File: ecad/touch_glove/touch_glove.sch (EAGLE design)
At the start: 181 parts, among them Q1 MCH3474 4A/30V/50mΩ, Q2 MCH3474 4A/30V/50mΩ, Q3 MCH3474 4A/30V/50mΩ, Q4 MCH3474 4A/30V/50mΩ, Q5 MCH3474 4A/30V/50mΩ, Q6 MCH3474 4A/30V/50mΩ, SW1 4A/28V, Y2 16MHz

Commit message: Rev 2: Complete transformation.  Start by replacing parts with new 3D models and new packages.
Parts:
- removed C135: 0.1uF/50V, PiB_capacitors:0.1UF_SMD-0402_50V-10%
- removed C136: 1uF/25V, PiB_capacitors:1UF_CER_SMD-0402_25V-10%
- added C11, C15, C23: 0.1uF/50V, PiB_capacitors:0.1UF_SMD-0402_50V-10%
- added C19, C24: 10uF/6.3V, PiB_capacitors:10UF_CER_SMD-0402_6.3V-20%
- added C28: 0.1uF/25V, PiB_capacitors:0.1UF_SMD-603_50V-20%
- added R45: 1KΩ, PiB_resistors:1KΩ_SMD-0603_1/10W-5%
- added U1: (no value), PiB:CD74HC4067-SM96_16:1_MUX-DEMUX_16:1-MUX-DEMUX
- added VREG2: 3.3V/250mA, PiB_ic_power:VREG_LINEAR_MCP1700_SOT-23
- added VREG3: 5A/5V, PiB_ic_power:VREG_MIC29501-5.0_LINEAR_ULDO_5A-5VMIC29501-5.0_5A-5V
- added VREG4: (no value), PiB_ic_power:VREG_LINEAR_MCP1700_SOT-23_
- A6: value 2.4GHz/802.11/0.5dBi/3W -> 2.45GHz; device PiB_radio_frequency:ANTENNA_SMD-CHIP_2.4GHZ-0.5DBI-3W -> PiB_radio_frequency:ANTENNA_SMD_CHP-2.45GHZ-0.5DBI-3W
- B2: value Impedence UNBAL/BAL (50Ω/100Ω) -> 50/100
- C10, C120, C123, C126, C14, C18, C22, C27, C37, C39, C43, C44, C97, C99: value 10uF/10V -> 10uF/6.3V; device PiB_capacitors:10UF_CER_SMD-0402_10V-20% -> PiB_capacitors:10UF_CER_SMD-0402_6.3V-20%
- C114: value 22pF/50V -> 22pF/100V; device PiB_capacitors:22PF_SMD-0402_100V-5% -> PiB_capacitors:22PF_CER_SMD-0402-100V-5%
- C115: device PiB_capacitors:0.75PF_SMD-0402_50V-33% -> PiB_capacitors:0.75PF_CER_SMD-0402_50V-33%
- D1, D11, D12, D2, D3, D4, D5: device PiB_discrete_semiconductors:DIODE_GENERAL-PURPOSE_SMD-0402_GP_120MA-75V -> PiB_discrete_semiconductors:DIODE_GENERAL-PURPOSE_SMD-0402_GP_150MA-75V
- DEMUX1: device PiB:CD74HC4067-SM96_16:1_MUX-DEMUX -> PiB:CD74HC4067-SM96_16:1_MUX-DEMUX_SOP-24_16:1-MUX-DEMUX
- JP2: value FTDIPTH-RA -> (none)
- L3, L4: value 10uH/0.38A -> 10uH/380mA
- MCU: value ATMEGA128RFA1 -> ATMEGA128RFA1_VFQFN-64_NO-EXPOSED-PAD; device PiB_ic_microcontrollers:ATMEGA128RFA1_VFQFN-64_EXPOSED-PAD -> PiB_ic_microcontrollers:ATMEGA128RFA1_VFQFN-64_NO-EXPOSED-PAD
- PWM_DRIVER1: device PiB:PCA9685_16-CH_12-BIT_PWM-DRIVER -> PiB:PCA9685_16-CH_12-BIT_PWM-DRIVER_TSSOP-28_PWM-DRIVER_16CH
- R10, R13, R15, R17, R19, R21, R23, R25, R27, R29, R31, R33, R6, R7, R8, R9: value 100Ω -> 100
- R11, R34, R35, R36, R37, R38, R39, R42, R43, R44: value 47KΩ -> 47K
- R40, R41: value 4.7KΩ -> 4.7K
- R48: value 2KΩ -> 2K
- R49: value 1KΩ -> 1K
- VREG1: device PiB_ic_power:VREG_TPS76833_ULDO_FAST-TRANSIENT_1A-3.3VTPS76833QDR_1A-3.3V -> PiB_ic_power:VREG_TPS768XX_ULDO_FAST-TRANSIENT_TPS76833QDR_1A-3.3V
- VREG7: device PiB_ic_power:VREG_LT1764EQ_ULDO_FAST-TRANSIENT_LT1764EQ-1.8_3A-1.8V -> PiB_ic_power:VREG_LT1764EQ_ULDO_FAST-TRANSIENT_LT1764EQ-1.8_3A_1.8V
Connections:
- new net N$33: C15.1, C19.1, L3.2, VREG4.VI
- new net N$34: R45.2, U1.C14
- net AGND: now also C23.2, C24.2; no longer C135.2, C136.2
- net AVCC: now also C23.1, C24.1, VREG4.VO; no longer C135.1, C136.1, L3.2, MCU.AREF
- net BATT_+: now also SW1.S1, U1.S1; no longer SW1.1
- net GND: now also C15.2, C19.2, JP2.GND, VREG4.GND; no longer JP2.6
- net N$10: now also HBRIDGE4.IN1/PH; no longer HBRIDGE4.IN1
- net N$13: now also HBRIDGE3.IN2/EN; no longer HBRIDGE3.IN2
- net N$14: now also HBRIDGE3.IN1/PH; no longer HBRIDGE3.IN1
- net N$19: now also HBRIDGE2.IN2/EN; no longer HBRIDGE2.IN2
- net N$20: now also HBRIDGE2.IN1/PH; no longer HBRIDGE2.IN1
- net N$25: now also HBRIDGE1.IN2/EN; no longer HBRIDGE1.IN2
- net N$26: now also HBRIDGE1.IN1/PH; no longer HBRIDGE1.IN1
- net N$29: now also HBRIDGE5.IN2/EN; no longer HBRIDGE5.IN2
- net N$31: now also HBRIDGE5.IN1/PH; no longer HBRIDGE5.IN1
- net N$44: now also Y2.XTAL2; no longer Y2.2
- net N$45: now also B2.OUT1; no longer B2.OUT2
- net N$46: now also B2.OUT2; no longer B2.OUT1
- net N$48: now also Y2.XTAL1; no longer Y2.1
- net N$50: now also JP2.DTR; no longer JP2.2
- net N$8: now also HBRIDGE4.IN2/EN; no longer HBRIDGE4.IN2
- net RX0: now also JP2.TXO; no longer JP2.4
- net TX0: now also JP2.RXI; no longer JP2.3
- net VBATT: now also SW1.P; no longer SW1.2
- net VCC: now also JP2.VCC; no longer JP2.1
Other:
- moved on the sheet: JP2, L3, VREG7

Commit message: Several more replacements and moved parts such that they are snapped to the grid.
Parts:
- removed C11: 0.1uF/50V, PiB_capacitors:0.1UF_SMD-0402_50V-10%
- removed C28: 0.1uF/25V, PiB_capacitors:0.1UF_SMD-603_50V-20%
- removed R45: 1KΩ, PiB_resistors:1KΩ_SMD-0603_1/10W-5%
- removed U1: (no value), PiB:CD74HC4067-SM96_16:1_MUX-DEMUX_16:1-MUX-DEMUX
- removed VREG2: 3.3V/250mA, PiB_ic_power:VREG_LINEAR_MCP1700_SOT-23
- removed VREG3: 5A/5V, PiB_ic_power:VREG_MIC29501-5.0_LINEAR_ULDO_5A-5VMIC29501-5.0_5A-5V
- C41: value 47uF/10V -> 47uF/6.3V; device PiB_capacitors:47UF_CER_SMD-0805_10V-20% -> PiB_capacitors:47UF_SMD-0805_6.3V-20%
- Q1, Q2, Q3, Q4, Q5, Q6: value MCH3474 4A/30V/50mΩ -> MCH3474 4A/30V; device PiB_discrete_semiconductors:POWER_NCHAN_MCH3474 -> PiB_discrete_semiconductors:POWER_NCHAN_MCH3474_NMOS_4A-30V
- VREG4: value (none) -> 250mA/3.3V
- VREG6: device PiB_ic_power:VREG_LINEAR_FIXED_TL1963A-33_LDO_1.5A-3.3V -> PiB_ic_power:VREG_TL1963A-XX_1.5A_LN_LDO_FAST-TRANSIENT_SOT-223-4_TL1963A-33_1.5A-3.3V
- Y2: value 16MHz -> 16 MHz
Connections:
- removed net N$34: R45.2, U1.C14
- removed net N$44: C113.1, MCU.XTAL1, Y2.XTAL2
- removed net N$48: C112.1, MCU.XTAL2, Y2.XTAL1
- new net N$35: C112.1, MCU.XTAL2, Y2.XTAL2
- new net N$36: C113.1, MCU.XTAL1, Y2.XTAL1
- net BATT_+: no longer U1.S1
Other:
- moved on the sheet: Y2

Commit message: Start and complete much of the 4 layer routing.  All components on board have 3D models.
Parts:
- removed ANALOG_BR: 2PT_GND_TIE, PiB_power_symbols:2PT_GND_TIE
- removed BATT2: BATTERYPTH_HOLES, PiB:BATTERYPTH_HOLES
- removed C1, C3, C4, C5, C6, C7: 0.1uF/50V, PiB_capacitors:0.1UF_SMD-0402_50V-10%
- removed C10, C14, C18, C22, C27: 10uF/6.3V, PiB_capacitors:10UF_CER_SMD-0402_6.3V-20%
- added LIPO1: Molex RA 2mm pitch, PiB_batteries:BATTERY-CONNECTOR_MOLEX_89401_RA-MALE_PITCH-2MM
- AVR_ISP: value AVR ISP -> AVRISP; device PiB_connectors:AVR_SPI_PRG_6NS -> PiB_connectors:AVR_SPI_PRG_6_PTH_VERT-MALE
- FLEX1, FLEX3, FLEX5, FLEX7, FLEX9: device PiB:FLEX-SENSOR10K_2.2IN -> PiB_sensors:FSR_FORCE-SENSATIVE-RESISTOR_PRESS-SENSOR_0530480210_RA-MALE_PITCH-1.25MM
- FLEX100, FLEX2, FLEX4, FLEX6, FLEX8: device PiB:FLEX-SENSOR10K_2.2IN -> PiB_sensors:FSR_FORCE-SENSATIVE-RESISTOR_PRESS-SENSOR_0530470210_VERT-MALE_PITCH-1.25MM
- HBRIDGE1, HBRIDGE2, HBRIDGE3, HBRIDGE4, HBRIDGE5: value DRV8837C -> DRV8837C 1A
- JP2: value (none) -> FTDI; device PiB_connectors:FTDIPTH-RA -> PiB_connectors:FTDI_PTH_RA-MALE
- TEC1, TEC2, TEC3, TEC4, TEC5: value PELTIER -> Molex RA 1.25mm pitch; device PiB:PELTIER-TECNL1025T_1.8A-4.4V_L10.7-W8.8-H2 -> PiB_actuators:PELTIER-TEC_CONNECTOR_0530480210_RA-MALE_PITCH-1.25MM
- VIBE1, VIBE2, VIBE3, VIBE4, VIBE5, VIBE6: value VIBE_MOTOR -> Molex RA 1.25mm pitch; device PiB:VIBE_MOTOR_100MA/3V -> PiB_actuators:VIBE-MOTOR_CONNECTOR_0530480210_RA-MALE_PITCH-1.25MM
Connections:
- removed net BATT_+: BATT2.P, SW1.S1
- removed net C10: DEMUX1.C10
- removed net C11: DEMUX1.C11
- removed net C12: DEMUX1.C12
- removed net C13: DEMUX1.C13
- removed net C8: DEMUX1.C8
- removed net C9: DEMUX1.C9
- removed net N$52: ANALOG_BR.P$1, L4.2
- new net +: LIPO1.+, SW1.S1
- net 1.8V: no longer C10.1, C14.1, C18.1, C22.1, C27.1
- net 3.3V: no longer C1.1, C3.1, C4.1, C5.1, C6.1, C7.1
- net A0: now also DEMUX1.SIG
- net A1: no longer DEMUX1.SIG
- net AGND: now also B2.GND@5, C110.2, C114.2, C115.2, DEMUX1.C10, DEMUX1.C11, DEMUX1.C12, DEMUX1.C13, DEMUX1.C14, DEMUX1.C15, L4.2, MCU.AVSS_RFN, MCU.AVSS_RFP; no longer ANALOG_BR.P$2
- net GND: now also AVR_ISP.GND, LIPO1.-, R1.1, R12.1, R2.1, R3.1, R4.1, R5.1; no longer AVR_ISP.6, B2.GND@5, BATT2.N, C110.2, C114.2, C115.2, MCU.AVSS_RFN, MCU.AVSS_RFP
- net MISO: now also AVR_ISP.MISO; no longer AVR_ISP.1
- net MOSI: now also AVR_ISP.MOSI; no longer AVR_ISP.4
- net N$15: no longer C4.2
- net N$17: no longer C3.2
- net N$2: no longer C6.2
- net N$3: no longer C7.2
- net N$30: no longer C1.2
- net N$4: no longer C5.2
- net NGND: no longer C10.2, C14.2, C18.2, C22.2, C27.2, R1.1, R12.1, R2.1, R3.1, R4.1, R5.1
- net PD4: now also DEMUX1.S0; no longer DEMUX1.S3
- net PD5: now also DEMUX1.S1; no longer DEMUX1.S2
- net PD6: now also DEMUX1.S3; no longer DEMUX1.S1
- net PD7: now also DEMUX1.S2; no longer DEMUX1.S0
- net RESET: now also AVR_ISP.RESET; no longer AVR_ISP.5
- net SCK: now also AVR_ISP.SCK; no longer AVR_ISP.3
- net STRAIN_1: now also DEMUX1.C4; no longer DEMUX1.C0
- net STRAIN_10: now also DEMUX1.C8; no longer DEMUX1.C15
- net STRAIN_2: now also DEMUX1.C9; no longer DEMUX1.C1
- net STRAIN_3: now also DEMUX1.C5; no longer DEMUX1.C2
- net STRAIN_4: now also DEMUX1.C0; no longer DEMUX1.C3
- net STRAIN_5: now also DEMUX1.C6; no longer DEMUX1.C4
- net STRAIN_6: now also DEMUX1.C1; no longer DEMUX1.C5
- net STRAIN_7: now also DEMUX1.C7; no longer DEMUX1.C6
- net STRAIN_8: now also DEMUX1.C2; no longer DEMUX1.C7
- net STRAIN_9: now also DEMUX1.C3; no longer DEMUX1.C14
- net TEC_1_COLD: now also PWM_DRIVER1.PWM7; no longer PWM_DRIVER1.PWM6
- net TEC_1_HOT: now also PWM_DRIVER1.PWM6; no longer PWM_DRIVER1.PWM7
- net VCC: no longer AVR_ISP.2, JP2.VCC
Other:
- moved on the sheet: D1, D12, D2, D3, D4, D5, VREG7

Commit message: Add option to use two different analog voltages.
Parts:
- removed A6: 2.45GHz, PiB_radio_frequency:ANTENNA_SMD_CHP-2.45GHZ-0.5DBI-3W
- removed B2: 50/100, PiB_radio_frequency:BALUN_SMD-0805_UNBAL/BAL-50/100
- removed C100, C106, C108, C116, C117, C119, C122, C124, C127, C98: 0.1uF/50V, PiB_capacitors:0.1UF_SMD-0402_50V-10%
- removed C107, C109, C110, C111, C132, C134: 1uF/25V, PiB_capacitors:1UF_CER_SMD-0402_25V-10%
- removed C112, C113: 12pF/100V, PiB_capacitors:12PF_SMD-0402_100V-5%
- removed C114: 22pF/100V, PiB_capacitors:22PF_CER_SMD-0402-100V-5%
- removed C115: 0.75pF/50V, PiB_capacitors:0.75PF_CER_SMD-0402_50V-33%
- removed C118: 100uF/16V, PiB_capacitors:100UF_CER_SMD-1210_16V-20%
- removed C120, C123, C126, C97, C99: 10uF/6.3V, PiB_capacitors:10UF_CER_SMD-0402_6.3V-20%
- removed D11, D12: 150mA/75V, PiB_discrete_semiconductors:DIODE_GENERAL-PURPOSE_SMD-0402_GP_150MA-75V
- removed D13, D14: 1A/50V, PiB_discrete_semiconductors:DIODE_GENERAL-PURPOSE_SMD_GP_1A-50V
- removed FLEX1, FLEX3, FLEX5, FLEX7, FLEX9: 10K, PiB_sensors:FSR_FORCE-SENSATIVE-RESISTOR_PRESS-SENSOR_0530480210_RA-MALE_PITCH-1.25MM
- removed FLEX100, FLEX2, FLEX4, FLEX6, FLEX8: 10K, PiB_sensors:FSR_FORCE-SENSATIVE-RESISTOR_PRESS-SENSOR_0530470210_VERT-MALE_PITCH-1.25MM
- removed HBRIDGE1, HBRIDGE2, HBRIDGE3, HBRIDGE4, HBRIDGE5: DRV8837C 1A, PiB:DRV883X_H-BRIDGE_DRV8837C_1A
- removed JP2: FTDI, PiB_connectors:FTDI_PTH_RA-MALE
- removed L3, L4: 10uH/380mA, PiB_inductors:10UH_SMD-0603_0.38A-0.468OHM-10%
- removed NOISE_BR: 2PT_GND_TIE, PiB_power_symbols:2PT_GND_TIE
- removed R49: 1K, PiB_resistors:1KΩ_SMD-0402_1/16W-5%
- removed TEC1, TEC2, TEC3, TEC4, TEC5: Molex RA 1.25mm pitch, PiB_actuators:PELTIER-TEC_CONNECTOR_0530480210_RA-MALE_PITCH-1.25MM
- removed VIBE1, VIBE2, VIBE3, VIBE4, VIBE5, VIBE6: Molex RA 1.25mm pitch, PiB_actuators:VIBE-MOTOR_CONNECTOR_0530480210_RA-MALE_PITCH-1.25MM
- removed VREG1: 1A/3.3V, PiB_ic_power:VREG_TPS768XX_ULDO_FAST-TRANSIENT_TPS76833QDR_1A-3.3V
- removed VREG4: 250mA/3.3V, PiB_ic_power:VREG_LINEAR_MCP1700_SOT-23_
- removed VREG6: TL1963A-33 1.5A/3.3V, PiB_ic_power:VREG_TL1963A-XX_1.5A_LN_LDO_FAST-TRANSIENT_SOT-223-4_TL1963A-33_1.5A-3.3V
- removed VREG7: 3A/1.8V, PiB_ic_power:VREG_LT1764EQ_ULDO_FAST-TRANSIENT_LT1764EQ-1.8_3A_1.8V
- removed Y2: 16 MHz, PiB:CRYSTAL_ABM3B_16MHZ_18PF
- added ANT1: 2.45GHz, PiB_radio_frequency:ANTENNA_SMD_CHP-2.45GHZ-0.5DBI-3W
- added BALUN1: 50/100, PiB_radio_frequency:BALUN_SMD-0805_UNBAL/BAL-50/100
- added BR_ANALOG, BR_NOISE: 2PT_GND_TIE, PiB_power_symbols:2PT_GND_TIE
- added C1, C3: 100uF/16V, PiB_capacitors:100UF_CER_SMD-1210_16V-20%
- added C10, C14, C22, C27, C5, C52, C53, C54, C55, C56, C57, C58, C59, C60, C7: 0.1uF/50V, PiB_capacitors:0.1UF_SMD-0402_50V-10%
- added C11, C4, C6: 10uF/6.3V, PiB_capacitors:10UF_CER_SMD-0402_6.3V-20%
- added C18: 47uF/6.3V, PiB_capacitors:47UF_SMD-0805_6.3V-20%
- added C28, C29: 1uF/25V, PiB_capacitors:1UF_CER_SMD-0402_25V-10%
- added C35: 0.75pF/50V, PiB_capacitors:0.75PF_CER_SMD-0402_50V-33%
- added D10, D6, D7, D9: 150mA/75V, PiB_discrete_semiconductors:DIODE_GENERAL-PURPOSE_SMD-0402_GP_150MA-75V
- added FLEX-INDEX, FLEX-MIDDLE, FLEX-PINKY, FLEX-RING, FLEX-THUMB: 10K, PiB_sensors:FSR_FORCE-SENSATIVE-RESISTOR_PRESS-SENSOR_0530480210_RA-MALE_PITCH-1.25MM
- added FLEX-INDEX2, FLEX-MIDDLE2, FLEX-PINKY2, FLEX-RING2, FLEX-THUMB2: 10K, PiB_sensors:FSR_FORCE-SENSATIVE-RESISTOR_PRESS-SENSOR_0530470210_VERT-MALE_PITCH-1.25MM
- added FTDI: FTDI, PiB_connectors:FTDI_PTH_RA-MALE
- added HBRIDGE-INDEX, HBRIDGE-MIDDLE, HBRIDGE-PINKY, HBRIDGE-RING, HBRIDGE-THUMB: DRV8837C 1A, PiB:DRV883X_H-BRIDGE_DRV8837C_1A
- added JP1: JUMPER-SMT_3_NO_SILK, PiB_connectors:JUMPER-SMT_3_NO_SILK
- added L1, L2: 10uH/380mA, PiB_inductors:10UH_SMD-0603_0.38A-0.468OHM-10%
- added R45: 10KΩ, PiB_resistors:10KΩ_SMD-0402_1/16W-5%
- added TEC-INDEX, TEC-MIDDLE, TEC-PINKY, TEC-RING, TEC-THUMB: Molex RA 1.25mm pitch, PiB_actuators:PELTIER-TEC_CONNECTOR_0530480210_RA-MALE_PITCH-1.25MM
- added VIBE-INDEX, VIBE-MIDDLE, VIBE-PALM, VIBE-PINKY, VIBE-RING, VIBE-THUMB: Molex RA 1.25mm pitch, PiB_actuators:VIBE-MOTOR_CONNECTOR_0530480210_RA-MALE_PITCH-1.25MM
- added VREG-ANALOG: 250mA/3.3V, PiB_ic_power:VREG_LINEAR_MCP1700_SOT-23_
- added VREG-MCU: 1A/3.3V, PiB_ic_power:VREG_TPS768XX_ULDO_FAST-TRANSIENT_TPS76833QDR_1A-3.3V
- added VREG-TEC: 3A/1.8V, PiB_ic_power:VREG_LT1764EQ_ULDO_FAST-TRANSIENT_LT1764EQ-1.8_3A_1.8V
- added VREG-VIBE: TL1963A-33 1.5A/3.3V, PiB_ic_power:VREG_TL1963A-XX_1.5A_LN_LDO_FAST-TRANSIENT_SOT-223-4_TL1963A-33_1.5A-3.3V
- added Y1: 16 MHz, PiB:CRYSTAL_ABM3B_16MHZ_18PF
- C12, C15, C17, C20, C49, C8: value 0.1uF/50V -> 10uF/6.3V; device PiB_capacitors:0.1UF_SMD-0402_50V-10% -> PiB_capacitors:10UF_CER_SMD-0402_6.3V-20%
- C19, C39, C43, C44: value 10uF/6.3V -> 0.1uF/50V; device PiB_capacitors:10UF_CER_SMD-0402_6.3V-20% -> PiB_capacitors:0.1UF_SMD-0402_50V-10%
- C21: value 0.1uF/50V -> 100uF/16V; device PiB_capacitors:0.1UF_SMD-0402_50V-10% -> PiB_capacitors:100UF_CER_SMD-1210_16V-20%
- C24: value 10uF/6.3V -> 1uF/25V; device PiB_capacitors:10UF_CER_SMD-0402_6.3V-20% -> PiB_capacitors:1UF_CER_SMD-0402_25V-10%
- C26, C31, C32: value 0.1uF/50V -> 1uF/25V; device PiB_capacitors:0.1UF_SMD-0402_50V-10% -> PiB_capacitors:1UF_CER_SMD-0402_25V-10%
- C33, C34: value 0.1uF/50V -> 12pF/100V; device PiB_capacitors:0.1UF_SMD-0402_50V-10% -> PiB_capacitors:12PF_SMD-0402_100V-5%
- C36: value 0.1uF/50V -> 22pF/100V; device PiB_capacitors:0.1UF_SMD-0402_50V-10% -> PiB_capacitors:22PF_CER_SMD-0402-100V-5%
- C41: value 47uF/6.3V -> 0.1uF/50V; device PiB_capacitors:47UF_SMD-0805_6.3V-20% -> PiB_capacitors:0.1UF_SMD-0402_50V-10%
- C42, C46: value 100uF/16V -> 0.1uF/50V; device PiB_capacitors:100UF_CER_SMD-1210_16V-20% -> PiB_capacitors:0.1UF_SMD-0402_50V-10%
- D1, D2, D3: value 150mA/75V -> 1A/50V; device PiB_discrete_semiconductors:DIODE_GENERAL-PURPOSE_SMD-0402_GP_150MA-75V -> PiB_discrete_semiconductors:DIODE_GENERAL-PURPOSE_SMD_GP_1A-50V
- D8: value 1A/50V -> 150mA/75V; device PiB_discrete_semiconductors:DIODE_GENERAL-PURPOSE_SMD_GP_1A-50V -> PiB_discrete_semiconductors:DIODE_GENERAL-PURPOSE_SMD-0402_GP_150MA-75V
- LED1: value GREEN -> BLUE; device PiB_leds:LED_SMD-0402_DISCRETE_GREEN -> PiB_leds:LED_SMD-0402_DISCRETE_BLUE
- LED2: value RED -> GREEN; device PiB_leds:LED_SMD-0402_DISCRETE_RED -> PiB_leds:LED_SMD-0402_DISCRETE_GREEN
- LED3: value BLUE -> RED; device PiB_leds:LED_SMD-0402_DISCRETE_BLUE -> PiB_leds:LED_SMD-0402_DISCRETE_RED
- R10, R13, R15, R6, R7, R8, R9: value 100 -> 47K; device PiB_resistors:100Ω_SMD-0402_1/16W-5% -> PiB_resistors:47KΩ_SMD-0402_1/16W-5%
- R12, R14: value 10KΩ -> 47K; device PiB_resistors:10KΩ_SMD-0402_1/16W-5% -> PiB_resistors:47KΩ_SMD-0402_1/16W-5%
- R16, R18, R20, R22, R24, R26, R28, R30: value 10KΩ -> 100; device PiB_resistors:10KΩ_SMD-0402_1/16W-5% -> PiB_resistors:100Ω_SMD-0402_1/16W-5%
- R2, R3: value 10KΩ -> 4.7K; device PiB_resistors:10KΩ_SMD-0402_1/16W-5% -> PiB_resistors:4.7KΩ_SMD-0402_1/16W-5%
- R33: value 100 -> 10KΩ; device PiB_resistors:100Ω_SMD-0402_1/16W-5% -> PiB_resistors:10KΩ_SMD-0402_1/16W-5%
- R34, R35, R36, R37, R38, R39, R42, R43, R44: value 47K -> 10KΩ; device PiB_resistors:47KΩ_SMD-0402_1/16W-5% -> PiB_resistors:10KΩ_SMD-0402_1/16W-5%
- R4: value 10KΩ -> 1K; device PiB_resistors:10KΩ_SMD-0402_1/16W-5% -> PiB_resistors:1KΩ_SMD-0402_1/16W-5%
- R40, R41: value 4.7K -> 10KΩ; device PiB_resistors:4.7KΩ_SMD-0402_1/16W-5% -> PiB_resistors:10KΩ_SMD-0402_1/16W-5%
- R48: value 2K -> 10KΩ; device PiB_resistors:2KΩ_SMD-0402_1/16W-5% -> PiB_resistors:10KΩ_SMD-0402_1/16W-5%
- R5: value 10KΩ -> 2K; device PiB_resistors:10KΩ_SMD-0402_1/16W-5% -> PiB_resistors:2KΩ_SMD-0402_1/16W-5%
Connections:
- removed net N$49: A6.SIGNAL, B2.IN, C115.1
- removed net STRAIN_1: DEMUX1.C4, FLEX1.-, R34.2
- removed net STRAIN_10: DEMUX1.C8, FLEX100.-, R38.2
- removed net STRAIN_2: DEMUX1.C9, FLEX2.-, R39.2
- removed net STRAIN_3: DEMUX1.C5, FLEX3.-, R35.2
- removed net STRAIN_4: DEMUX1.C0, FLEX4.-, R42.2
- removed net STRAIN_5: DEMUX1.C6, FLEX5.-, R36.2
- removed net STRAIN_6: DEMUX1.C1, FLEX6.-, R43.2
- removed net STRAIN_7: DEMUX1.C7, FLEX7.-, R37.2
- removed net STRAIN_8: DEMUX1.C2, FLEX8.-, R44.2
- removed net STRAIN_9: DEMUX1.C3, FLEX9.-, R11.2
- removed net TEC_1_COLD: PWM_DRIVER1.PWM7, R27.1
- removed net TEC_1_HOT: PWM_DRIVER1.PWM6, R29.1
- removed net TEC_2_COLD: PWM_DRIVER1.PWM14, R23.1
- removed net TEC_2_HOT: PWM_DRIVER1.PWM15, R25.1
- removed net TEC_3_COLD: PWM_DRIVER1.PWM12, R19.1
- removed net TEC_3_HOT: PWM_DRIVER1.PWM13, R21.1
- removed net TEC_4_COLD: PWM_DRIVER1.PWM10, R15.1
- removed net TEC_4_HOT: PWM_DRIVER1.PWM11, R17.1
- removed net TEC_5_COLD: PWM_DRIVER1.PWM8, R31.1
- removed net TEC_5_HOT: PWM_DRIVER1.PWM9, R33.1
- removed net VIBE_1: PWM_DRIVER1.PWM0, R6.1
- removed net VIBE_2: PWM_DRIVER1.PWM1, R7.1
- removed net VIBE_3: PWM_DRIVER1.PWM2, R8.1
- removed net VIBE_4: PWM_DRIVER1.PWM3, R9.1
- removed net VIBE_5: PWM_DRIVER1.PWM4, R10.1
- removed net VIBE_6: PWM_DRIVER1.PWM5, R13.1
- new net FLEX-INDEX1: DEMUX1.C6, FLEX-INDEX.-, R7.2
- new net FLEX-INDEX2: DEMUX1.C1, FLEX-INDEX2.-, R12.2
- new net FLEX-MIDDLE1: DEMUX1.C5, FLEX-MIDDLE.-, R8.2
- new net FLEX-MIDDLE2: DEMUX1.C0, FLEX-MIDDLE2.-, R13.2
- new net FLEX-PINKY1: DEMUX1.C3, FLEX-PINKY.-, R10.2
- new net FLEX-PINKY2: DEMUX1.C8, FLEX-PINKY2.-, R15.2
- new net FLEX-RING1: DEMUX1.C4, FLEX-RING.-, R9.2
- new net FLEX-RING2: DEMUX1.C9, FLEX-RING2.-, R14.2
- new net FLEX-THUMB1: DEMUX1.C7, FLEX-THUMB.-, R6.2
- new net FLEX-THUMB2: DEMUX1.C2, FLEX-THUMB2.-, R11.2
- new net N$40: BR_ANALOG.P$2, L1.1
- new net RFSIG: ANT1.SIGNAL, BALUN1.IN, C35.1
- new net TEC-INDEX-COLD: PWM_DRIVER1.PWM10, R25.1
- new net TEC-INDEX-HOT: PWM_DRIVER1.PWM11, R24.1
- new net TEC-MIDDLE-COLD: PWM_DRIVER1.PWM12, R27.1
- new net TEC-MIDDLE-HOT: PWM_DRIVER1.PWM13, R26.1
- new net TEC-PINKY-COLD: PWM_DRIVER1.PWM7, R31.1
- new net TEC-PINKY-HOT: PWM_DRIVER1.PWM6, R30.1
- new net TEC-RING-COLD: PWM_DRIVER1.PWM14, R29.1
- new net TEC-RING-HOT: PWM_DRIVER1.PWM15, R28.1
- new net TEC-THUMB-COLD: PWM_DRIVER1.PWM8, R23.1
- new net TEC-THUMB-HOT: PWM_DRIVER1.PWM9, R22.1
- new net VIBE-INDEX: PWM_DRIVER1.PWM4, R20.1
- new net VIBE-MIDDLE: PWM_DRIVER1.PWM3, R19.1
- new net VIBE-PALM: PWM_DRIVER1.PWM0, R16.1
- new net VIBE-PINKY: PWM_DRIVER1.PWM1, R17.1
- new net VIBE-RING: PWM_DRIVER1.PWM2, R18.1
- new net VIBE-THUMB: PWM_DRIVER1.PWM5, R21.1
- new net VSENSOR: C37.1, C38.1, C39.1, C40.1, C41.1, C42.1, C43.1, C44.1, C45.1, C46.1, C47.1, C48.1, DEMUX1.VCC, FLEX-INDEX.+, FLEX-INDEX2.+, FLEX-MIDDLE.+, FLEX-MIDDLE2.+, FLEX-PINKY.+, FLEX-PINKY2.+, FLEX-RING.+, FLEX-RING2.+, FLEX-THUMB.+, FLEX-THUMB2.+, JP1.2
- net +: now also SW1.P; no longer SW1.S1
- net 1.8V: now also C19.1, C20.1, C56.1, C57.1, C58.1, C59.1, C60.1, D3.A, HBRIDGE-INDEX.VM, HBRIDGE-MIDDLE.VM, HBRIDGE-PINKY.VM, HBRIDGE-RING.VM, HBRIDGE-THUMB.VM, VREG-TEC.SENSE, VREG-TEC.VOUT; no longer C13.1, C17.1, C26.1, C39.1, C40.1, C42.1, C9.1, D14.A, HBRIDGE1.VM, HBRIDGE2.VM, HBRIDGE3.VM, HBRIDGE4.VM, HBRIDGE5.VM, VREG7.SENSE, VREG7.VOUT
- net 3.3V: now also C16.1, C17.1, C18.1, D10.K, D2.A, D6.K, D7.K, D8.K, D9.K, VIBE-INDEX.+, VIBE-MIDDLE.+, VIBE-PALM.+, VIBE-PINKY.+, VIBE-RING.+, VIBE-THUMB.+, VREG-VIBE.VO; no longer C36.1, C41.1, C43.1, D1.K, D12.K, D13.A, D2.K, D3.K, D4.K, VIBE1.+, VIBE2.+, VIBE3.+, VIBE4.+, VIBE5.+, VIBE6.+, VREG6.VO
- net AGND: now also BALUN1.GND@5, C14.2, C15.2, C29.2, C35.2, C36.2, C37.2, C38.2, C39.2, C40.2, C41.2, C42.2, C43.2, C44.2, C45.2, C46.2, L1.2, R10.1, R12.1, R13.1, R14.1, R15.1, R6.1, R7.1, R8.1, R9.1; no longer B2.GND@5, C100.2, C110.2, C114.2, C115.2, C122.2, C134.2, C23.2, C24.2, C32.2, C33.2, C34.2, C49.2, C50.2, C51.2, C97.2, L4.2, R34.1, R35.1, R36.1, R37.1, R38.1, R39.1, R42.1, R43.1, R44.1
- net AVCC: now also C29.1, JP1.3, L2.2; no longer C100.1, C122.1, C134.1, C23.1, C24.1, C31.1, C32.1, C33.1, C34.1, C47.1, C48.1, C49.1, C50.1, C51.1, C97.1, DEMUX1.VCC, FLEX1.+, FLEX100.+, FLEX2.+, FLEX3.+, FLEX4.+, FLEX5.+, FLEX6.+, FLEX7.+, FLEX8.+, FLEX9.+, VREG4.VO
- net GND: now also BR_ANALOG.P$1, BR_NOISE.P$2, C10.2, C11.2, C13.2, C23.2, C24.2, C26.2, C27.2, C28.2, C32.2, C33.2, C34.2, C49.2, C50.2, C51.2, C52.2, C53.2, C54.2, C55.2, FTDI.GND, R33.1, R34.1, R35.1, R36.1, R37.1, R38.1, R39.1, R40.1, R41.1, R42.1, R43.1, R44.1, R45.1, R46.1, VREG-ANALOG.GND, VREG-MCU.!EN, VREG-MCU.GND; no longer C106.2, C107.2, C108.2, C109.2, C111.2, C112.2, C113.2, C116.2, C118.2, C119.2, C120.2, C123.2, C124.2, C126.2, C127.2, C132.2, C15.2, C16.2, C19.2, C2.2, C20.2, C37.2, C38.2, C44.2, C45.2, C46.2, C8.2, C98.2, C99.2, JP2.GND, L4.1, NOISE_BR.P$2, R1.1, R12.1, R14.1, R16.1, R18.1, R2.1, R20.1, R22.1, R24.1, R26.1, R28.1, R3.1, R30.1, R48.1, R49.1, VREG1.!EN, VREG1.GND, VREG4.GND
- net N$1: now also HBRIDGE-THUMB.OUT2, TEC-THUMB.HOT; no longer HBRIDGE5.OUT2, TEC5.HOT
- net N$10: now also HBRIDGE-INDEX.IN1/PH, R24.2, R40.2; no longer HBRIDGE4.IN1/PH, R16.2, R17.2
- net N$11: now also HBRIDGE-INDEX.OUT2, TEC-INDEX.HOT; no longer HBRIDGE4.OUT2, TEC4.HOT
- net N$12: now also HBRIDGE-MIDDLE.OUT2, TEC-MIDDLE.HOT; no longer HBRIDGE3.OUT2, TEC3.HOT
- net N$13: now also HBRIDGE-MIDDLE.IN2/EN, R27.2, R43.2; no longer HBRIDGE3.IN2/EN, R18.2, R19.2
- net N$14: now also HBRIDGE-MIDDLE.IN1/PH, R26.2, R42.2; no longer HBRIDGE3.IN1/PH, R20.2, R21.2
- net N$15: now also D6.A, VIBE-PINKY.-; no longer D2.A, VIBE2.-
- net N$16: now also HBRIDGE-MIDDLE.OUT1, TEC-MIDDLE.COLD; no longer HBRIDGE3.OUT1, TEC3.COLD
- net N$17: now also D5.A, VIBE-PALM.-; no longer D1.A, VIBE1.-
- net N$18: now also HBRIDGE-RING.OUT2, TEC-RING.HOT; no longer HBRIDGE2.OUT2, TEC2.HOT
- net N$19: now also HBRIDGE-RING.IN2/EN, R29.2, R45.2; no longer HBRIDGE2.IN2/EN, R22.2, R23.2
- net N$2: now also D8.A, VIBE-MIDDLE.-; no longer D4.A, VIBE4.-
- net N$20: now also HBRIDGE-RING.IN1/PH, R28.2, R44.2; no longer HBRIDGE2.IN1/PH, R24.2, R25.2
- net N$21: now also R19.2, R35.2; no longer R4.2, R9.2
- net N$22: now also R20.2, R36.2; no longer R10.2, R5.2
- net N$23: now also HBRIDGE-RING.OUT1, TEC-RING.COLD; no longer HBRIDGE2.OUT1, TEC2.COLD
- net N$24: now also HBRIDGE-PINKY.OUT2, TEC-PINKY.HOT; no longer HBRIDGE1.OUT2, TEC1.HOT
- net N$25: now also HBRIDGE-PINKY.IN2/EN, R31.2, R47.2; no longer HBRIDGE1.IN2/EN, R26.2, R27.2
- net N$26: now also HBRIDGE-PINKY.IN1/PH, R30.2, R46.2; no longer HBRIDGE1.IN1/PH, R28.2, R29.2
- net N$27: now also HBRIDGE-PINKY.OUT1, TEC-PINKY.COLD; no longer HBRIDGE1.OUT1, TEC1.COLD
- net N$28: now also R16.2, R32.2; no longer R1.2, R6.2
- net N$29: now also HBRIDGE-THUMB.IN2/EN, R23.2, R39.2; no longer HBRIDGE5.IN2/EN, R30.2, R31.2
- net N$3: now also D9.A, VIBE-INDEX.-; no longer D5.A, VIBE5.-
- net N$30: now also D10.A, VIBE-THUMB.-; no longer D12.A, VIBE6.-
- net N$31: now also HBRIDGE-THUMB.IN1/PH, R22.2, R38.2; no longer HBRIDGE5.IN1/PH, R32.2, R33.2
- net N$32: now also R21.2, R37.2; no longer R12.2, R13.2
- net N$33: now also C14.1, JP1.1, VREG-ANALOG.VO; no longer C19.1, L3.2, VREG4.VI
- net N$35: now also C34.1, Y1.XTAL2; no longer C112.1, Y2.XTAL2
- net N$36: now also C33.1, Y1.XTAL1; no longer C113.1, Y2.XTAL1
- net N$4: now also D7.A, VIBE-RING.-; no longer D3.A, VIBE3.-
- net N$45: now also BALUN1.OUT1; no longer B2.OUT1
- net N$46: now also BALUN1.OUT2; no longer B2.OUT2
- net N$47: now also BALUN1.GND@2, C36.1; no longer B2.GND@2, C114.1
- net N$5: now also HBRIDGE-THUMB.OUT1, TEC-THUMB.COLD; no longer HBRIDGE5.OUT1, TEC5.COLD
- net N$50: now also C22.1, FTDI.DTR; no longer C117.1, JP2.DTR
- net N$53: now also LED1.K, R48.2; no longer LED3.K, R47.2
- net N$54: now also LED2.K, R4.2; no longer LED1.K, R49.2
- net N$55: now also LED3.K, R5.2; no longer LED2.K, R48.2
- net N$6: now also HBRIDGE-INDEX.OUT1, TEC-INDEX.COLD; no longer HBRIDGE4.OUT1, TEC4.COLD
- net N$62: now also C32.1; no longer C132.1
- net N$63: now also C31.1; no longer C110.1
- net N$7: now also R17.2, R33.2; no longer R2.2, R7.2
- net N$8: now also HBRIDGE-INDEX.IN2/EN, R25.2, R41.2; no longer HBRIDGE4.IN2/EN, R14.2, R15.2
- net N$9: now also R18.2, R34.2; no longer R3.2, R8.2
- net NGND: now also BR_NOISE.P$1, C1.2, C16.2, C18.2, C19.2, C2.2, C20.2, C3.2, C4.2, C5.2, C56.2, C57.2, C58.2, C59.2, C6.2, C60.2, C7.2, C8.2, HBRIDGE-INDEX.GND, HBRIDGE-MIDDLE.GND, HBRIDGE-PINKY.GND, HBRIDGE-RING.GND, HBRIDGE-THUMB.GND, R48.1, VREG-TEC.GND, VREG-VIBE.GND; no longer C13.2, C26.2, C36.2, C39.2, C40.2, C41.2, C42.2, C43.2, HBRIDGE1.GND, HBRIDGE2.GND, HBRIDGE3.GND, HBRIDGE4.GND, HBRIDGE5.GND, NOISE_BR.P$1, VREG6.GND, VREG7.GND
- net PB6: now also LED3.A; no longer LED2.A
- net PB7: now also LED2.A; no longer LED1.A
- net RESET: now also C22.2, D4.A, R1.1; no longer C117.2, D11.A, R46.1
- net RX0: now also FTDI.TXO; no longer JP2.TXO
- net SCL: now also R2.1; no longer R40.1
- net SDA: now also R3.1; no longer R41.1
- net TX0: now also FTDI.RXI; no longer JP2.RXI
- net VBATT: now also C1.1, C3.1, C4.1, C5.1, C6.1, C7.1, C8.1, C9.1, D1.K, D2.K, D3.K, LED1.A, SW1.S1, VREG-MCU.VIN, VREG-TEC.!SHDN, VREG-TEC.VIN, VREG-VIBE.VI; no longer C118.1, C119.1, C120.1, C126.1, C127.1, C37.1, C38.1, C44.1, C45.1, C46.1, D13.K, D14.K, D8.K, LED3.A, SW1.P, VREG1.VIN, VREG6.VI, VREG7.!SHDN, VREG7.VIN
- net VCC: now also C10.1, C11.1, C13.1, C23.1, C24.1, C26.1, C27.1, C28.1, C49.1, C50.1, C51.1, C52.1, C53.1, C54.1, C55.1, D1.A, D4.K, HBRIDGE-INDEX.NSLEEP, HBRIDGE-INDEX.VCC, HBRIDGE-MIDDLE.NSLEEP, HBRIDGE-MIDDLE.VCC, HBRIDGE-PINKY.NSLEEP, HBRIDGE-PINKY.VCC, HBRIDGE-RING.NSLEEP, HBRIDGE-RING.VCC, HBRIDGE-THUMB.NSLEEP, HBRIDGE-THUMB.VCC, L2.1, R1.2, R2.2, R3.2, VREG-ANALOG.VI, VREG-MCU.VOUT; no longer C106.1, C107.1, C108.1, C109.1, C111.1, C116.1, C123.1, C124.1, C16.1, C20.1, C8.1, C98.1, C99.1, D11.K, D8.A, HBRIDGE1.NSLEEP, HBRIDGE1.VCC, HBRIDGE2.NSLEEP, HBRIDGE2.VCC, HBRIDGE3.NSLEEP, HBRIDGE3.VCC, HBRIDGE4.NSLEEP, HBRIDGE4.VCC, HBRIDGE5.NSLEEP, HBRIDGE5.VCC, L3.1, R40.2, R41.2, R46.2, VREG1.VOUT
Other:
- note added: "Designed by: MrSwirlyEyes"
- note added: "Rev 2"
- note added: "TOUCH GLOVE"
- note removed: "ROBOTIC ARM"
- note removed: "Rev 1"
- note removed: "VIBROTACTILE DRIVERS"
- moved on the sheet: AVR_ISP, C12, C13, C15, C16, C17, C19, C2, C20, C21, C23, C24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

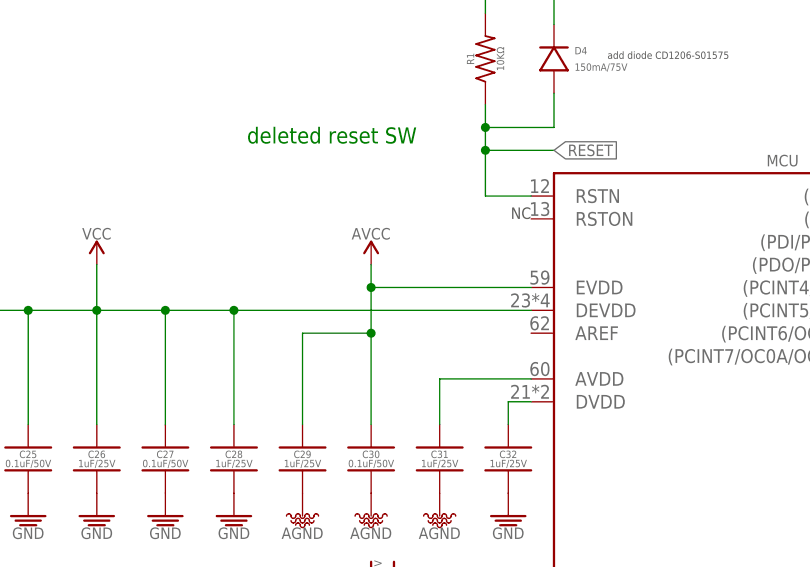
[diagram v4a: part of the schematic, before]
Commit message: Replaced Robotic Arm components for those with 3D models.  Also went down to 0402 component size.
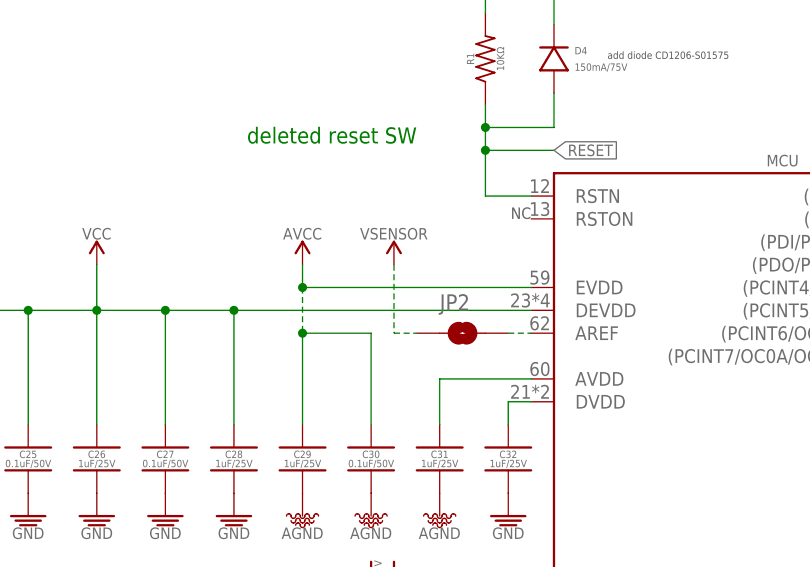
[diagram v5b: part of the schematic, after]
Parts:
- added JP2: JUMPER-SMT_2_NO_SILK, PiB_connectors:JUMPER-SMT_2_NO_SILK
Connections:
- new net N$39: JP2.2, MCU.AREF
- net VSENSOR: now also JP2.1
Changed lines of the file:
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@@
 <setting verticaltext="up"/>
 </settings>
-<grid distance="0.1" unitdist="inch" unit="inch" style="lines" multiple="1" display="yes" altdistance="0.01" altunitdist="inch" altunit="inch"/>
+<grid distance="0.1" unitdist="inch" unit="inch" style="lines" multiple="1" display="no" altdistance="0.01" altunitdist="inch" altunit="inch"/>
 <layers>
 <layer number="1" name="Top" color="4" fill="1" visible="no" active="no"/>
@@
 <part name="SUPPLY120" library="PiB_power_symbols" deviceset="VSENSOR" device=""/>
 <part name="SUPPLY121" library="PiB_power_symbols" deviceset="VSENSOR" device=""/>
+<part name="JP2" library="PiB_connectors" deviceset="JUMPER-SMT_2_NO" device="_SILK"/>
+<part name="SUPPLY13" library="PiB_power_symbols" deviceset="VSENSOR" device=""/>
 </parts>
 <sheets>
@@
 <instance part="NGND25" gate="G$1" x="312.42" y="403.86"/>
 <instance part="GND139" gate="GND" x="408.94" y="91.44"/>
-<instance part="SUPPLY126" gate="G$1" x="312.42" y="431.8"/>
+<instance part="SUPPLY126" gate="G$1" x="304.8" y="431.8"/>
 <instance part="BR_NOISE" gate="G$1" x="264.16" y="251.46"/>
 <instance part="LED1" gate="G$1" x="314.96" y="276.86"/>
@@
 <instance part="SUPPLY120" gate="G$1" x="492.76" y="447.04"/>
 <instance part="SUPPLY121" gate="G$1" x="502.92" y="447.04"/>
+<instance part="JP2" gate="G$1" x="322.58" y="424.18"/>
+<instance part="SUPPLY13" gate="G$1" x="314.96" y="431.8"/>
 </instances>
 <busses>
@@
 <wire x1="304.8" y1="424.18" x2="312.42" y2="424.18" width="0.1524" layer="91"/>
 <pinref part="SUPPLY126" gate="G$1" pin="AVCC"/>
-<wire x1="312.42" y1="431.8" x2="312.42" y2="429.26" width="0.1524" layer="91"/>
+<wire x1="304.8" y1="431.8" x2="304.8" y2="429.26" width="0.1524" layer="91"/>
 <pinref part="MCU" gate="G$1" pin="EVDD"/>
-<wire x1="330.2" y1="429.26" x2="312.42" y2="429.26" width="0.1524" layer="91"/>
+<wire x1="330.2" y1="429.26" x2="304.8" y2="429.26" width="0.1524" layer="91"/>
 <pinref part="C29" gate="G$1" pin="1"/>
 <wire x1="304.8" y1="414.02" x2="304.8" y2="424.18" width="0.1524" layer="91"/>
 <pinref part="C30" gate="G$1" pin="1"/>
 <wire x1="312.42" y1="414.02" x2="312.42" y2="424.18" width="0.1524" layer="91"/>
-<wire x1="312.42" y1="424.18" x2="312.42" y2="429.26" width="0.1524" layer="91"/>
-<junction x="312.42" y="424.18"/>
-<junction x="312.42" y="429.26"/>
+<junction x="304.8" y="429.26"/>
+<wire x1="304.8" y1="429.26" x2="304.8" y2="424.18" width="0.1524" layer="91" style="longdash"/>
+<junction x="304.8" y="424.18"/>
 </segment>
 <segment>
@@
 <pinref part="SUPPLY121" gate="G$1" pin="VSENSOR"/>
 </segment>
+<segment>
+<pinref part="SUPPLY13" gate="G$1" pin="VSENSOR"/>
+<wire x1="314.96" y1="431.8" x2="314.96" y2="424.18" width="0.1524" layer="91" style="longdash"/>
+<pinref part="JP2" gate="G$1" pin="1"/>
+<wire x1="314.96" y1="424.18" x2="317.5" y2="424.18" width="0.1524" layer="91" style="longdash"/>
+</segment>
+</net>
+<net name="N$39" class="0">
+<segment>
+<pinref part="JP2" gate="G$1" pin="2"/>
+<pinref part="MCU" gate="G$1" pin="AREF"/>
+<wire x1="327.66" y1="424.18" x2="330.2" y2="424.18" width="0.1524" layer="91" style="longdash"/>
+</segment>
 </net>
